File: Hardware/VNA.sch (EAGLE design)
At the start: 453 parts, among them IC1 LTC5510, IC10 LT5560, IC11 LTC6362, IC12 MCP33131D-10-E/MS, IC13 SI5351C, IC14 MAX2871, IC15 NCP702-3.3, IC16 RFSW6042, IC17 AP2114H, IC18 RFSW6042, IC19 MAX2871, IC2 LT5560, IC20 NCP702-3.3, IC21 AP2114H, IC22 F2912, IC23 F1958, IC24 TRF37A73, IC25 F2912, IC26 F2912, IC27 F2912, IC28 LDL212PU50R, IC29 LDL212PU50R, IC3 LTC6362, IC30 LDL212PU50R, IC31 LDL212PU50R, IC32 TPS65265, IC33 STM32L432KC, IC34 NCP702-1.8, IC35 NCP702-1.8, IC36 NCP702-1.8, IC4 MCP33131D-10-E/MS, IC5 LTC5510, IC6 LT5560, IC7 LTC6362, IC8 MCP33131D-10-E/MS, IC9 LTC5510, J1 U.FL-R-SMT, J2 U.FL-R-SMT, J3 DCJ0202, Q1 FA-128 26MHz, T1 MABA011082, T2 MABA011082, T3 MABA011082, U2 6SLX9TQG144, U4 W25Q16BVSN, X1 RLB DUT/RF IN, X2 RLB DUT/RF IN, X4 MINI-USB-SCHIELD-32005-301

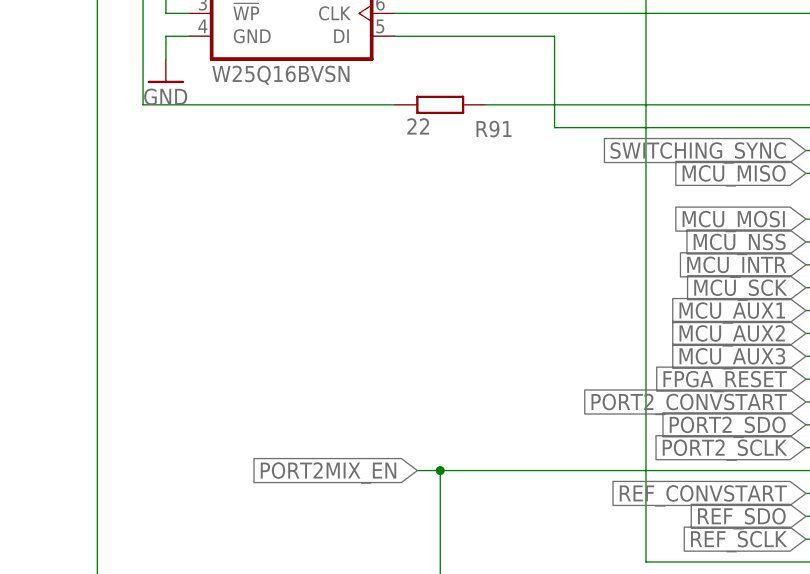
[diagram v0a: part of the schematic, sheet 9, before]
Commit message: Various minor improvements and bugfixes/workarounds for HW mistakes
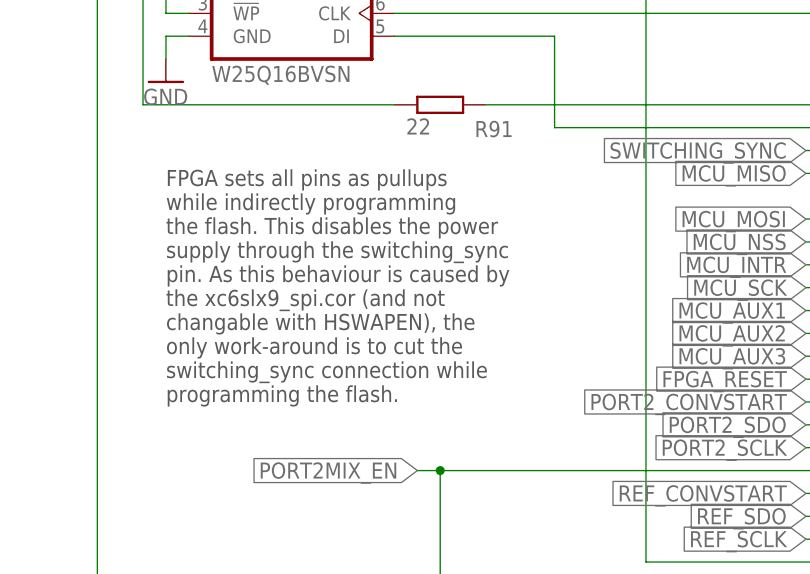
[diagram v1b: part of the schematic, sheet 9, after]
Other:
- note added: "FPGA sets all pins as pullups while indirectly programming the flash. This disables the power supply through the switching_sync pin. As this behaviour is caused by the xc6slx9_spi.cor (and not changable with HSWAPEN), the only work-around is to cut the switching_sync connection while programming the flash."
- note added: "Mistake: place compensation R/C in series"
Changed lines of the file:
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@@
 <text x="30.48" y="53.34" size="1.778" layer="97">Resistor set for 1MHz, can be overwritten by signal at ROSC</text>
 <text x="53.34" y="200.66" size="1.778" layer="97">Regulators on with floating enable</text>
+<text x="27.94" y="157.48" size="1.778" layer="97">Mistake: place compensation R/C in series</text>
+<text x="27.94" y="116.84" size="1.778" layer="97">Mistake: place compensation R/C in series</text>
+<text x="30.48" y="195.58" size="1.778" layer="97">Mistake: place compensation R/C in series</text>
 </plain>
 <instances>
@@
 <plain>
 <text x="345.44" y="20.32" size="1.778" layer="94">FPGA + MCU Connections</text>
+<text x="246.38" y="172.72" size="1.778" layer="97">FPGA sets all pins as pullups
+while indirectly programming
+the flash. This disables the power
+supply through the switching_sync
+pin. As this behaviour is caused by
+the xc6slx9_spi.cor (and not
+changable with HSWAPEN), the
+only work-around is to cut the
+switching_sync connection while
+programming the flash.</text>
 </plain>
 <instances>

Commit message: Bugfixes
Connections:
- net FILT_IN_C1: now also R99.2, U2B3.IO_L44P_GCLK21_3; no longer R100.2, U2B3.IO_L43N_GCLK22_IRDY2_3
- net FILT_IN_C2: now also R100.2, U2B3.IO_L43N_GCLK22_IRDY2_3; no longer R99.2, U2B3.IO_L44P_GCLK21_3
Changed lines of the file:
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@@
 </segment>
 </net>
-<net name="FILT_IN_C1" class="0">
+<net name="FILT_IN_C2" class="0">
 <segment>
 <pinref part="R100" gate="G$1" pin="2"/>
@@
 </segment>
 </net>
-<net name="FILT_IN_C2" class="0">
+<net name="FILT_IN_C1" class="0">
 <segment>
 <pinref part="R99" gate="G$1" pin="2"/>
@@
 </segment>
 </net>
-<net name="FILT_IN_C1" class="0">
+<net name="FILT_IN_C2" class="0">
 <segment>
 <pinref part="U2" gate="B3" pin="IO_L43N_GCLK22_IRDY2_3"/>
@@
 </segment>
 </net>
-<net name="FILT_IN_C2" class="0">
+<net name="FILT_IN_C1" class="0">
 <segment>
 <pinref part="U2" gate="B3" pin="IO_L44P_GCLK21_3"/>

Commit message: Part values of final IF filter adjusted
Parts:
- C16, C17, C19, C60, C61, C62, C92, C93, C94: value 22n -> 330p
- C27, C53, C85: value 4n7 -> 330p
- L19, L20, L29, L30, L4, L5: value 4u7 -> 220Ohm
- R17, R18, R29, R30: value 620 -> 6k8
- R19, R20, R31, R32, R47, R48: value 33 -> 220
- R45, R46: value 200 -> 4k7

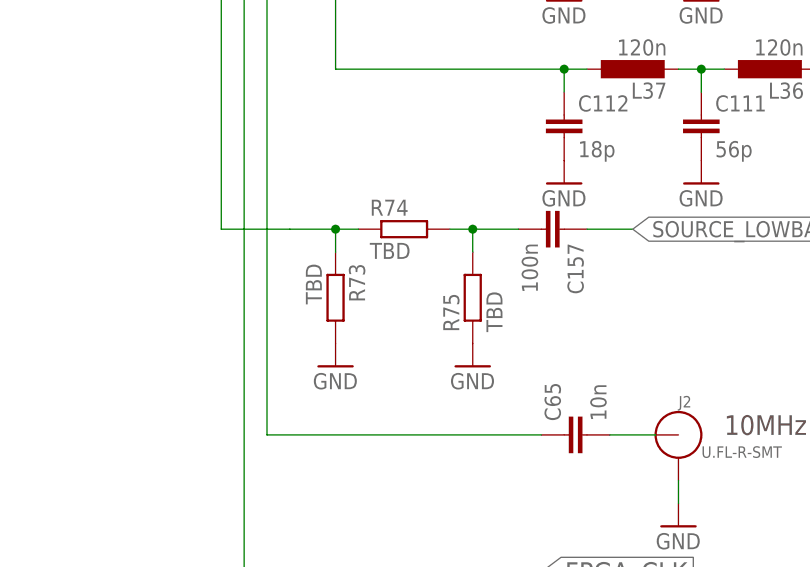
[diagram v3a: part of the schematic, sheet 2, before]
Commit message: Lowband source implemented, faster algorithm for PLL divider selection
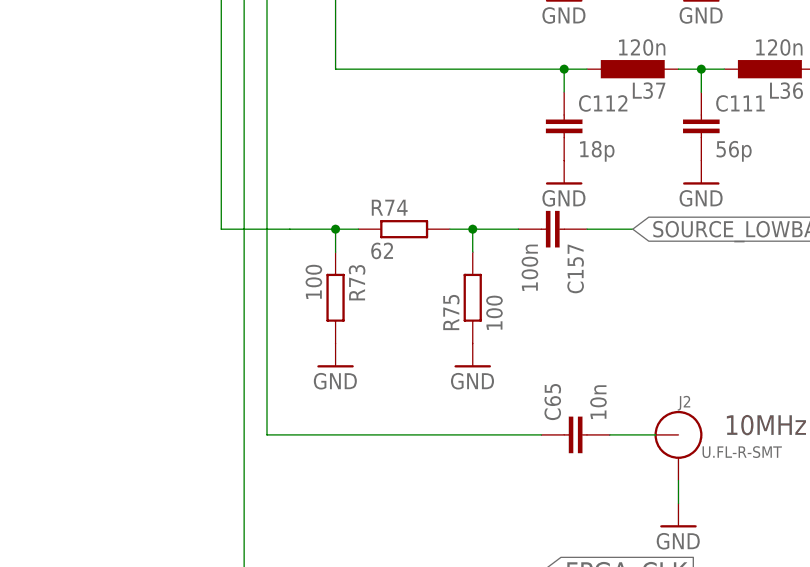
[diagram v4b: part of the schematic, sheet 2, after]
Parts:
- R73, R75: value TBD -> 100
- R74: value TBD -> 62
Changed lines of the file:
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@@
 <part name="GND164" library="VNA" library_urn="urn:adsk.eagle:library:19762030" deviceset="GND" device=""/>
 <part name="GND165" library="VNA" library_urn="urn:adsk.eagle:library:19762030" deviceset="GND" device=""/>
-<part name="R73" library="VNA" library_urn="urn:adsk.eagle:library:19762030" deviceset="R-EU_" device="R0603" package3d_urn="urn:adsk.eagle:package:19762122/2" value="TBD"/>
-<part name="R74" library="VNA" library_urn="urn:adsk.eagle:library:19762030" deviceset="R-EU_" device="R0603" package3d_urn="urn:adsk.eagle:package:19762122/2" value="TBD"/>
-<part name="R75" library="VNA" library_urn="urn:adsk.eagle:library:19762030" deviceset="R-EU_" device="R0603" package3d_urn="urn:adsk.eagle:package:19762122/2" value="TBD"/>
+<part name="R73" library="VNA" library_urn="urn:adsk.eagle:library:19762030" deviceset="R-EU_" device="R0603" package3d_urn="urn:adsk.eagle:package:19762122/2" value="100"/>
+<part name="R74" library="VNA" library_urn="urn:adsk.eagle:library:19762030" deviceset="R-EU_" device="R0603" package3d_urn="urn:adsk.eagle:package:19762122/2" value="62"/>
+<part name="R75" library="VNA" library_urn="urn:adsk.eagle:library:19762030" deviceset="R-EU_" device="R0603" package3d_urn="urn:adsk.eagle:package:19762122/2" value="100"/>
 <part name="GND166" library="VNA" library_urn="urn:adsk.eagle:library:19762030" deviceset="GND" device=""/>
 <part name="GND167" library="VNA" library_urn="urn:adsk.eagle:library:19762030" deviceset="GND" device=""/>
